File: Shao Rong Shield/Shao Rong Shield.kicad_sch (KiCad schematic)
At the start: 12 parts, among them J1 Power, J10 VIBRATION MOTOR, J11 SPARE1, J12 SPARE2, J2 Digital/PWM, J3 Analog, J4 Digital/PWM, J5 POWER SUPPLY, J6 STEPPER MOTOR, J7 KEYBOARD, J8 LCD, J9 RS232

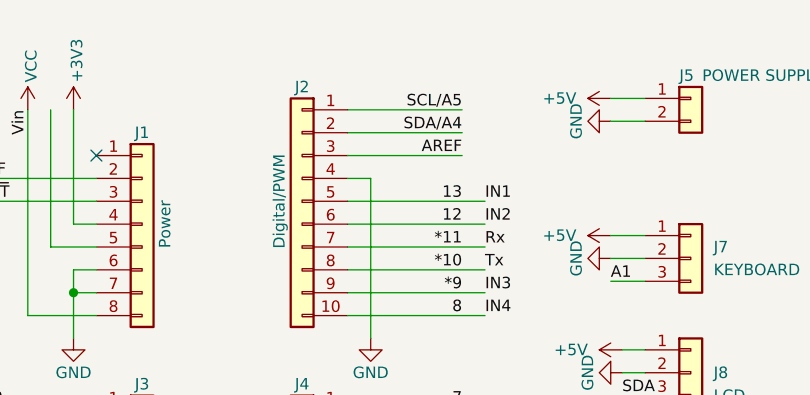
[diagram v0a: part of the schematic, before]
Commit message: Completed Shaorong and A4988 Shield
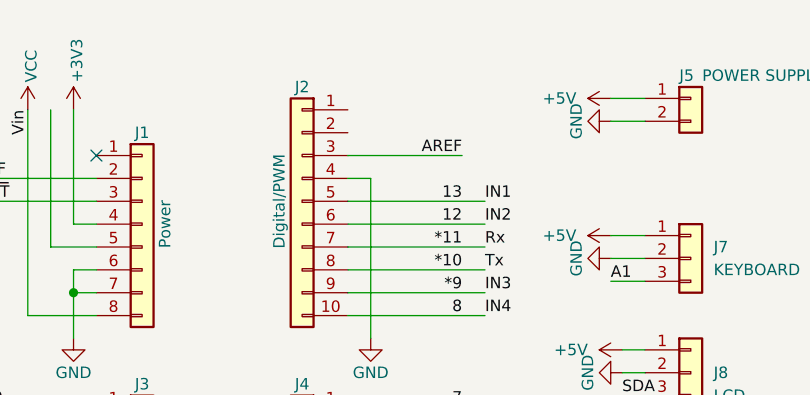
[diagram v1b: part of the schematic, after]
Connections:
- net SCL/A5: no longer J2.1 (Pin_1)
- net SDA: no longer J2.2 (Pin_2)
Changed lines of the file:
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@@
-	(wire
-		(pts
-			(xy 62.23 26.67) (xy 74.93 26.67)
-		)
-		(stroke
-			(width 0)
-			(type solid)
-		)
-	)
 	(wire
 		(pts
@@
 			(width 0)
 			(type default)
-		)
-	)
-	(wire
-		(pts
-			(xy 62.23 29.21) (xy 74.93 29.21)
-		)
-		(stroke
-			(width 0)
-			(type solid)
 		)
 	)
@@
 		)
 	)
-	(label "SDA{slash}A4"
-		(at 74.93 29.21 180)
-		(fields_autoplaced yes)
-		(effects
-			(font
-				(size 1.27 1.27)
-			)
-			(justify right bottom)
-		)
-	)
 	(label "8"
 		(at 74.93 49.53 180)
@@
 		(fields_autoplaced yes)
 		(effects
-			(font
-				(size 1.27 1.27)
-			)
-			(justify right bottom)
-		)
-	)
-	(label "SCL{slash}A5"
-		(at 74.93 26.67 180)
-		(fields_autoplaced yes)
-		(effects
